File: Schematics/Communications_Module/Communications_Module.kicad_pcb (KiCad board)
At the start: 4 copper layers, 69.5 x 60 mm, 72 parts, among them J1 USB_B_Micro, J2 SWD_01x04_Pin, J3 Stack Male Edge Connector, Q1 AO3400A, SW1 SW_STM_RESET, SW2 SW_STM_BOOT_MODE, U1 RFM95W-915S2, U2 W25Q128JVS, U3 AMS1117-3.3, U4 LM66100DCKR, U5 LM66100DCKR, U6 LM66100DCKR, U7 STM32F103CBT6, U8 ACS70331EOLC, U9 ISO1042BDWVR, Y1 X322516MMB4SI

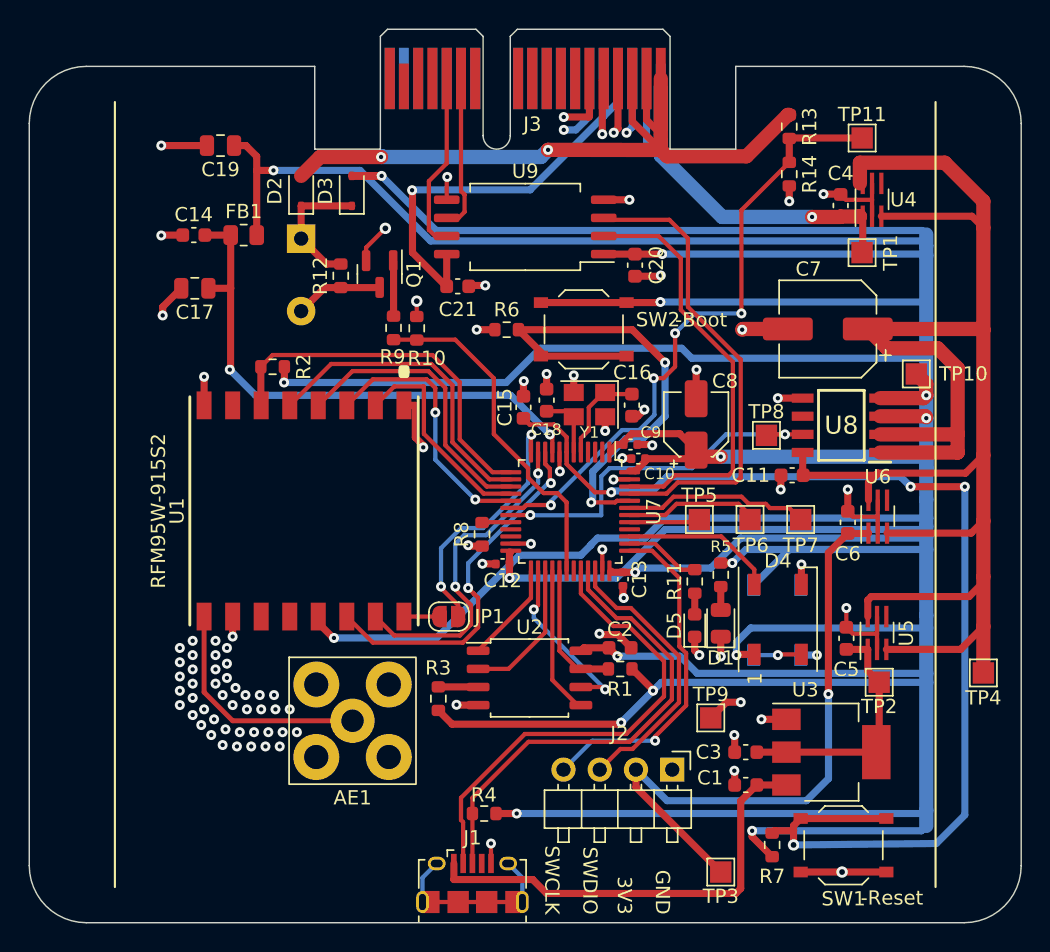
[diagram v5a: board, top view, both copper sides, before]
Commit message: Attempt at via stitching
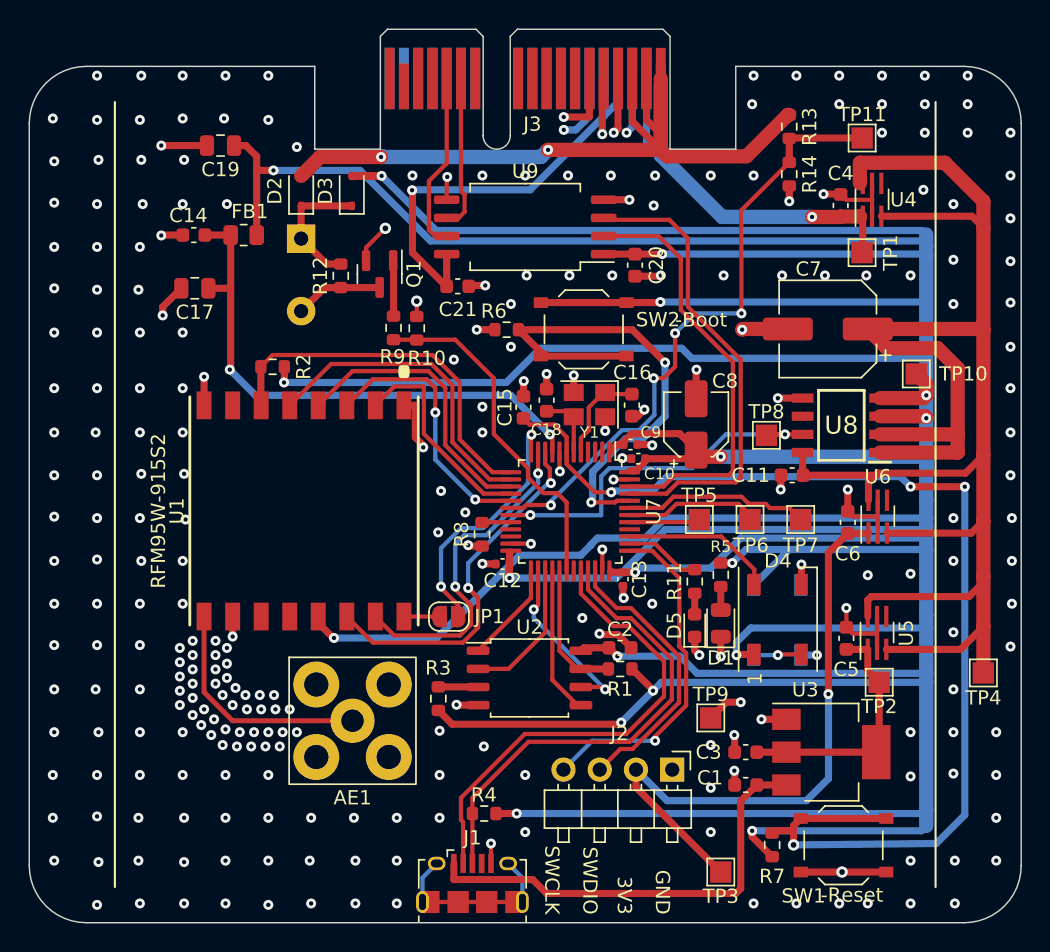
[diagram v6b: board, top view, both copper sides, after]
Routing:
- net GND: vias 95 -> 281
